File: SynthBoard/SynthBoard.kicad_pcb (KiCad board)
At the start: 2 copper layers, 160 x 80 mm, 113 parts, among them IC1 PIC16F15325-I/P, IC2 MCP6232T-E/SN, IC3 MCP6232T-E/SN, IC4 AS321KTR-E1, IC5 V3340M, IC6 AS321KTR-E1, IC7 4013, J1 Output, J2 Input, J3 Input, J4 Output, J6 A_Power, J7 D_Power, Q1 Q_NPN_ECB, Q18 Q_NPN_ECB, SW1 MFP_240, U1 NJM4558M

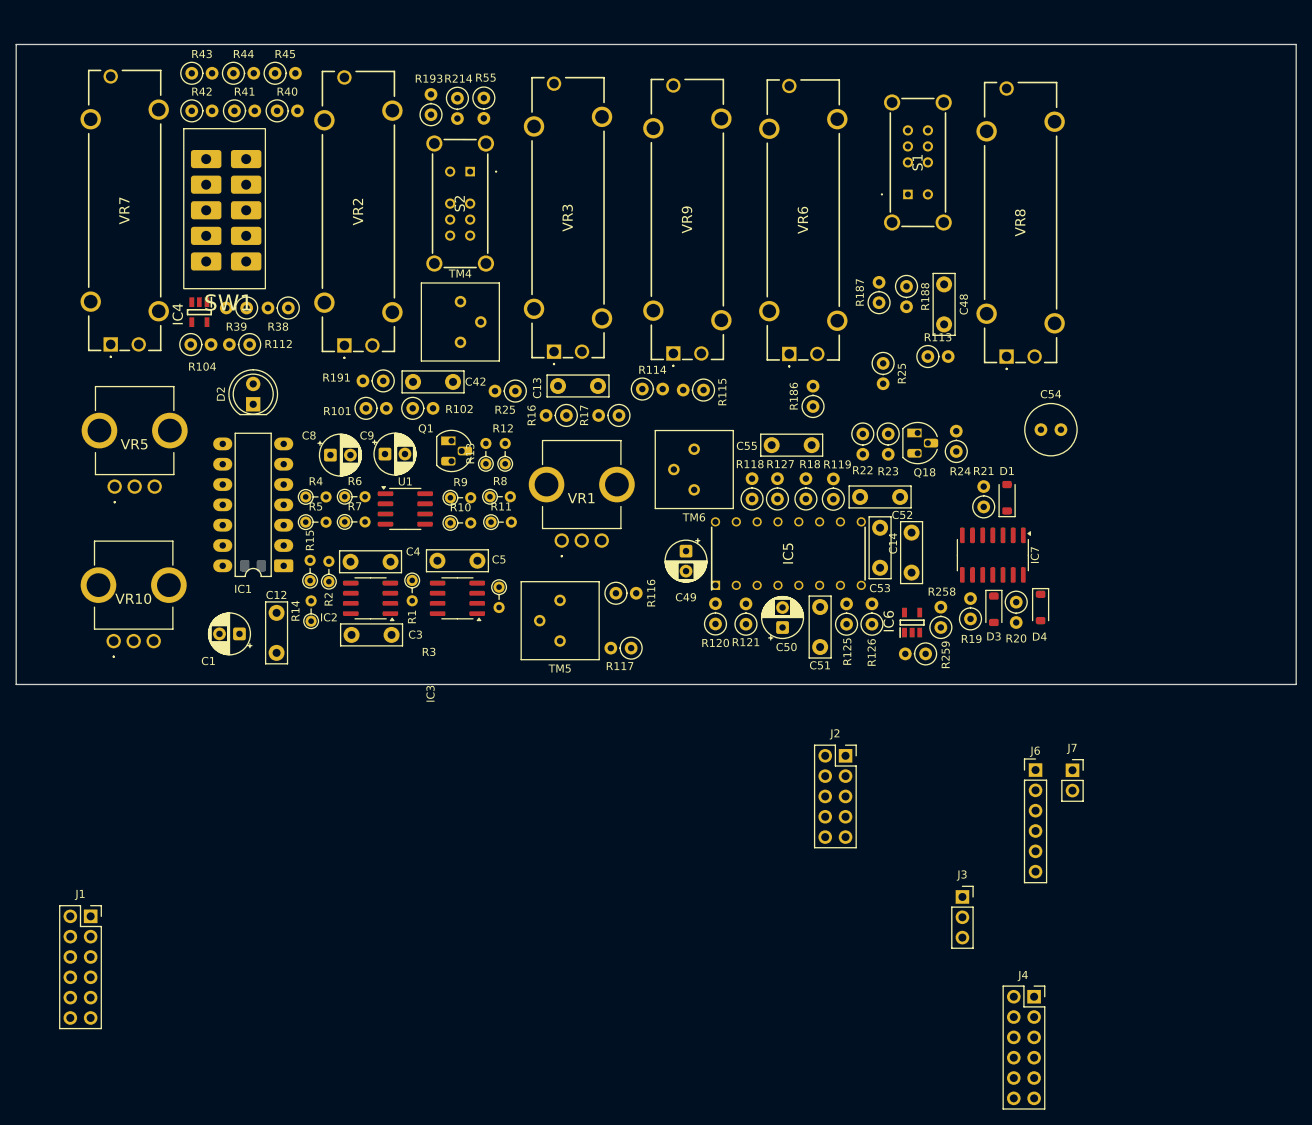
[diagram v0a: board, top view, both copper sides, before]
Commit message: SynthBoard
部品をSMDにしてVCO+LFOを配置した
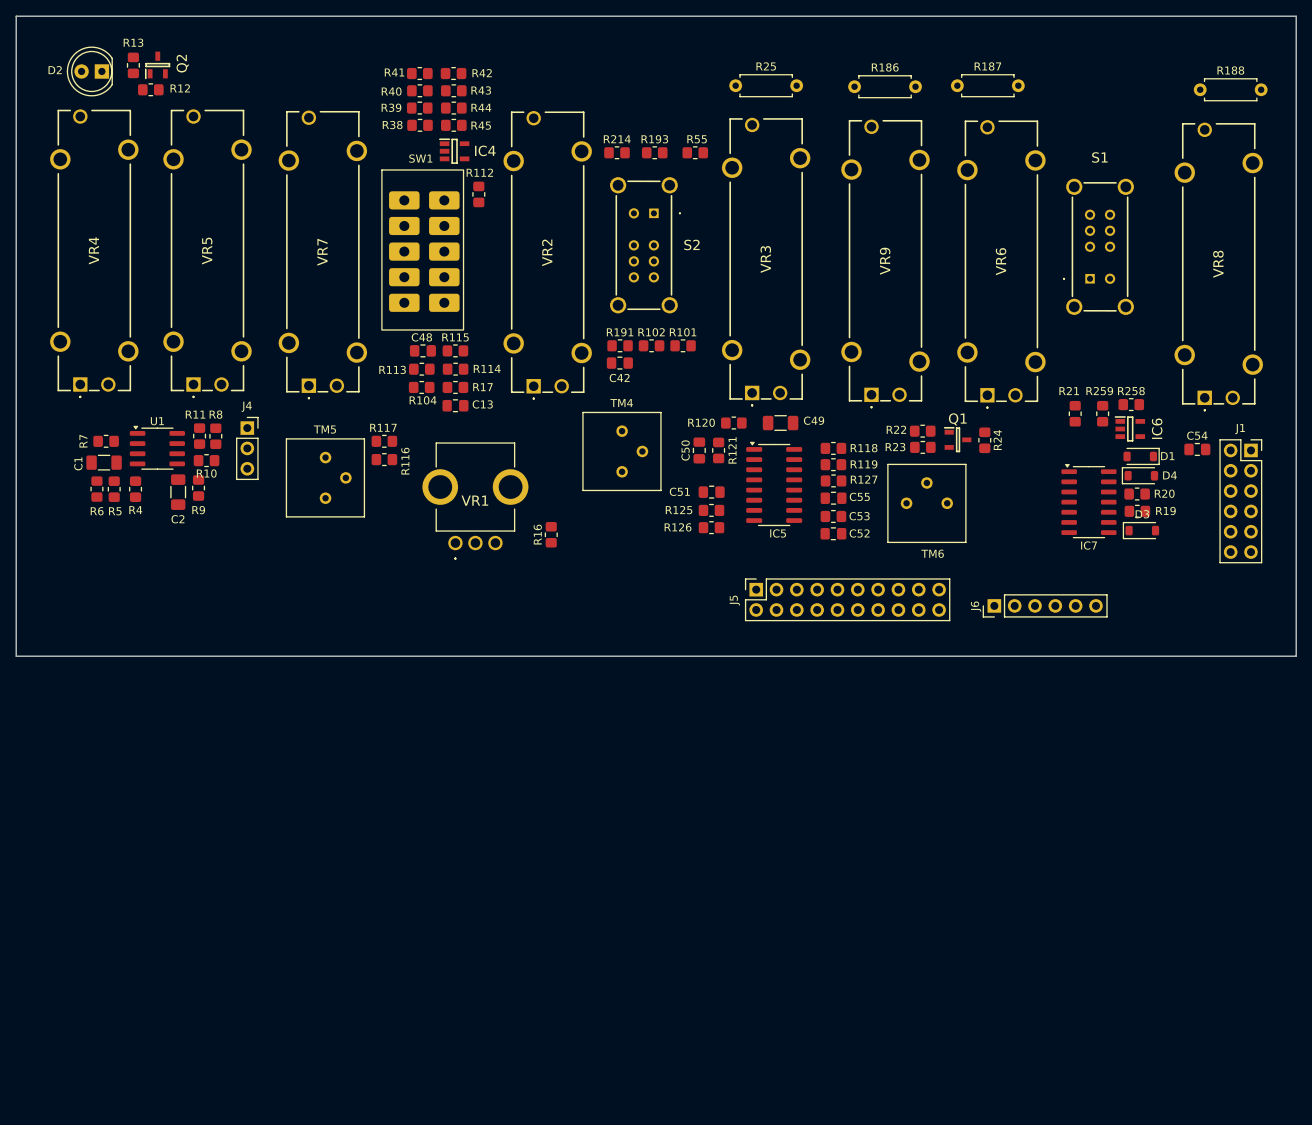
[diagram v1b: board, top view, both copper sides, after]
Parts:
- removed C11: 0.1uF, Capacitor_SMD:C_0805_2012Metric_Pad1.18x1.45mm_HandSolder
- removed C12, C14, C3, C4, C5: 0.01uF, Capacitor_THT:C_Disc_D7.5mm_W2.5mm_P5.00mm
- removed C8, C9: 47uF/16V, Capacitor_THT:CP_Radial_D5.0mm_P2.50mm
- removed IC1: PIC16F15325-I/P, Package_DIP:DIP-14_W7.62mm_LongPads
- removed IC2, IC3: MCP6232T-E/SN, Package_SO:SOIC-8_3.9x4.9mm_P1.27mm
- removed J2: Input, Connector_PinSocket_2.54mm:PinSocket_2x05_P2.54mm_Vertical
- removed J3: Input, Connector_PinSocket_2.54mm:PinSocket_1x03_P2.54mm_Vertical
- removed J7: D_Power, Connector_PinSocket_2.54mm:PinSocket_1x02_P2.54mm_Vertical
- removed Q18: Q_NPN_ECB, Package_TO_SOT_THT:TO-92_HandSolder
- removed R1, R2, R3: 10K, Resistor_THT:R_Axial_DIN0204_L3.6mm_D1.6mm_P2.54mm_Vertical
- removed R14: 1K, Resistor_THT:R_Axial_DIN0204_L3.6mm_D1.6mm_P2.54mm_Vertical
- removed R15: 100, Resistor_THT:R_Axial_DIN0204_L3.6mm_D1.6mm_P2.54mm_Vertical
- removed R18: 1M, Resistor_THT:R_Axial_DIN0207_L6.3mm_D2.5mm_P2.54mm_Vertical
- removed the R25 at (146.9, 86.4)
- removed the R25 at (101.0, 89.9)
- removed VR10: Delay 100KB, SamacSys_parts:RK09D117000B
- added C2: EMK316BBJ476ML-T, Capacitor_SMD:C_1206_3216Metric_Pad1.33x1.80mm_HandSolder, F.Cu at (58.8, 102.5)
- added J5: DigiConn, Connector_PinSocket_2.54mm:PinSocket_2x10_P2.54mm_Vertical, F.Cu at (131.1, 114.7)
- added Q2: 2SC1623(RANGE:300-400), SamacSys_parts:SOT95P237X125-3N, F.Cu at (56.3, 49.1)
- added R25: 390K, Resistor_THT:R_Axial_DIN0207_L6.3mm_D2.5mm_P7.62mm_Horizontal, F.Cu at (128.5, 51.7)
- added VR4: Rate 100KB, SamacSys_parts:PTA20432010CIB104, F.Cu at (46.6, 89.0)
- C1: value 10uF/16V -> EMK316BBJ476ML-T; footprint Capacitor_THT:CP_Radial_D5.0mm_P2.50mm -> Capacitor_SMD:C_1206_3216Metric_Pad1.33x1.80mm_HandSolder
- C13: value 0.001uF -> CL21C102JBCNNNC; footprint Capacitor_THT:C_Disc_D7.5mm_W2.5mm_P5.00mm -> Capacitor_SMD:C_0805_2012Metric_Pad1.18x1.45mm_HandSolder
- C42, C48, C55: value 0.01uF -> 0805B103J500NT; footprint Capacitor_THT:C_Disc_D7.5mm_W2.5mm_P5.00mm -> Capacitor_SMD:C_0805_2012Metric_Pad1.18x1.45mm_HandSolder
- C49: value 47uF/16V -> C3216X5R1E476MTJ00E; footprint Capacitor_THT:CP_Radial_D5.0mm_P2.50mm -> Capacitor_SMD:C_1206_3216Metric_Pad1.33x1.80mm_HandSolder
- C50: value 2.2uF/50V -> CL21B225KAFNNNE; footprint Capacitor_THT:CP_Radial_D5.0mm_P2.50mm -> Capacitor_SMD:C_0805_2012Metric_Pad1.18x1.45mm_HandSolder
- C51, C52: value 0.01uF -> CL21C102JBCNNNC; footprint Capacitor_THT:C_Disc_D7.5mm_W2.5mm_P5.00mm -> Capacitor_SMD:C_0805_2012Metric_Pad1.18x1.45mm_HandSolder
- C53: value 1000pF -> CL21C102JBCNNNC; footprint Capacitor_THT:C_Disc_D7.5mm_W2.5mm_P5.00mm -> Resistor_SMD:R_0805_2012Metric_Pad1.20x1.40mm_HandSolder
- C54: value 10uF/16VBP -> CL21A106KAYNNNE; footprint Capacitor_THT:C_Radial_D6.3mm_H7.0mm_P2.50mm -> Capacitor_SMD:C_0805_2012Metric_Pad1.18x1.45mm_HandSolder
- IC4, IC6: value AS321KTR-E1 -> AS321KTR-G1
- IC5: footprint SamacSys_parts:DIP794W56P260L1905H432Q16N -> Package_SO:SOP-16_3.9x9.9mm_P1.27mm
- IC7: value 4013 -> HEF4013BT,653
- J4: value Output -> Conn_01x03; footprint Connector_PinSocket_2.54mm:PinSocket_2x06_P2.54mm_Vertical -> Connector_PinSocket_2.54mm:PinSocket_1x03_P2.54mm_Vertical
- Q1: value Q_NPN_ECB -> 2SC1623(RANGE:300-400); footprint Package_TO_SOT_THT:TO-92L_HandSolder -> SamacSys_parts:SOT95P237X125-3N
- R10: value 10K -> 0805W8F1002T5E; footprint Resistor_THT:R_Axial_DIN0204_L3.6mm_D1.6mm_P2.54mm_Vertical -> Resistor_SMD:R_0805_2012Metric_Pad1.20x1.40mm_HandSolder
- R101: value 56K -> 0805W8J0563T5E; footprint Resistor_THT:R_Axial_DIN0207_L6.3mm_D2.5mm_P2.54mm_Vertical -> Resistor_SMD:R_0805_2012Metric_Pad1.20x1.40mm_HandSolder
- R102: value 390K -> 0805W8J0394T5E; footprint Resistor_THT:R_Axial_DIN0207_L6.3mm_D2.5mm_P2.54mm_Vertical -> Resistor_SMD:R_0805_2012Metric_Pad1.20x1.40mm_HandSolder
- R104: value 220K -> 0805W8F2203T5E; footprint Resistor_THT:R_Axial_DIN0207_L6.3mm_D2.5mm_P2.54mm_Vertical -> Resistor_SMD:R_0805_2012Metric_Pad1.20x1.40mm_HandSolder
- R11: value 1.2K -> 0805W8F1201T5E; footprint Resistor_THT:R_Axial_DIN0204_L3.6mm_D1.6mm_P2.54mm_Vertical -> Resistor_SMD:R_0805_2012Metric_Pad1.20x1.40mm_HandSolder
- R112, R114, R116, R191: value 100K -> 0805W8J0104T5E; footprint Resistor_THT:R_Axial_DIN0207_L6.3mm_D2.5mm_P2.54mm_Vertical -> Resistor_SMD:R_0805_2012Metric_Pad1.20x1.40mm_HandSolder
- R113, R127: value 560 -> 0805W8F5600T5E; footprint Resistor_THT:R_Axial_DIN0207_L6.3mm_D2.5mm_P2.54mm_Vertical -> Resistor_SMD:R_0805_2012Metric_Pad1.20x1.40mm_HandSolder
- R115: value 560K -> 0805W8F5603T5E; footprint Resistor_THT:R_Axial_DIN0207_L6.3mm_D2.5mm_P2.54mm_Vertical -> Resistor_SMD:R_0805_2012Metric_Pad1.20x1.40mm_HandSolder
- R117: value 270K -> 0805W8F2703T5E; footprint Resistor_THT:R_Axial_DIN0207_L6.3mm_D2.5mm_P2.54mm_Vertical -> Resistor_SMD:R_0805_2012Metric_Pad1.20x1.40mm_HandSolder
- R118: value 1.8K -> 0805W8F1801T5E; footprint Resistor_THT:R_Axial_DIN0207_L6.3mm_D2.5mm_P2.54mm_Vertical -> Resistor_SMD:R_0805_2012Metric_Pad1.20x1.40mm_HandSolder
- R119, R125: value 1.5M -> 0805W8F1504T5E; footprint Resistor_THT:R_Axial_DIN0207_L6.3mm_D2.5mm_P2.54mm_Vertical -> Resistor_SMD:R_0805_2012Metric_Pad1.20x1.40mm_HandSolder
- R12, R4, R9: value 100K -> 0805W8J0104T5E; footprint Resistor_THT:R_Axial_DIN0204_L3.6mm_D1.6mm_P2.54mm_Vertical -> Resistor_SMD:R_0805_2012Metric_Pad1.20x1.40mm_HandSolder
- R120: value 28K -> 0805W8F2802T5E; footprint Resistor_THT:R_Axial_DIN0207_L6.3mm_D2.5mm_P2.54mm_Vertical -> Resistor_SMD:R_0805_2012Metric_Pad1.20x1.40mm_HandSolder
- R121: value 5.6K -> 0805W8F5601T5E; footprint Resistor_THT:R_Axial_DIN0207_L6.3mm_D2.5mm_P2.54mm_Vertical -> Resistor_SMD:R_0805_2012Metric_Pad1.20x1.40mm_HandSolder
- R126, R16, R214, R22: value 10K -> 0805W8F1002T5E; footprint Resistor_THT:R_Axial_DIN0207_L6.3mm_D2.5mm_P2.54mm_Vertical -> Resistor_SMD:R_0805_2012Metric_Pad1.20x1.40mm_HandSolder
- R13: value 2.2K -> 0805W8F2201T5E; footprint Resistor_THT:R_Axial_DIN0204_L3.6mm_D1.6mm_P2.54mm_Vertical -> Resistor_SMD:R_0805_2012Metric_Pad1.20x1.40mm_HandSolder
- R17: value 1M -> 0805W8F1004T5E; footprint Resistor_THT:R_Axial_DIN0207_L6.3mm_D2.5mm_P2.54mm_Vertical -> Resistor_SMD:R_0805_2012Metric_Pad1.20x1.40mm_HandSolder
- R186, R187, R188: footprint Resistor_THT:R_Axial_DIN0207_L6.3mm_D2.5mm_P2.54mm_Vertical -> Resistor_THT:R_Axial_DIN0207_L6.3mm_D2.5mm_P7.62mm_Horizontal
- R19: value 47K -> 0805W8F4702T5E; footprint Resistor_THT:R_Axial_DIN0207_L6.3mm_D2.5mm_P2.54mm_Vertical -> Resistor_SMD:R_0805_2012Metric_Pad1.20x1.40mm_HandSolder
- R193, R259: value 33K -> 0805W8F3302T5E; footprint Resistor_THT:R_Axial_DIN0207_L6.3mm_D2.5mm_P2.54mm_Vertical -> Resistor_SMD:R_0805_2012Metric_Pad1.20x1.40mm_HandSolder
- R20, R21: value 47k -> 0805W8F4702T5E; footprint Resistor_THT:R_Axial_DIN0207_L6.3mm_D2.5mm_P2.54mm_Vertical -> Resistor_SMD:R_0805_2012Metric_Pad1.20x1.40mm_HandSolder
- R23: value 1K -> 0805W8F1001T5E; footprint Resistor_THT:R_Axial_DIN0207_L6.3mm_D2.5mm_P2.54mm_Vertical -> Resistor_SMD:R_0805_2012Metric_Pad1.20x1.40mm_HandSolder
- R24: value 68K -> 0805W8F6802T5E; footprint Resistor_THT:R_Axial_DIN0207_L6.3mm_D2.5mm_P2.54mm_Vertical -> Resistor_SMD:R_0805_2012Metric_Pad1.20x1.40mm_HandSolder
- R258: value 470k -> 0805w8f4703t5e; footprint Resistor_THT:R_Axial_DIN0207_L6.3mm_D2.5mm_P2.54mm_Vertical -> Resistor_SMD:R_0805_2012Metric_Pad1.20x1.40mm_HandSolder
- R38, R39, R40, R41, R42, R43, R44, R45: value 200K -> 0805W8F2003T5E; footprint Resistor_THT:R_Axial_DIN0207_L6.3mm_D2.5mm_P2.54mm_Vertical -> Resistor_SMD:R_0805_2012Metric_Pad1.20x1.40mm_HandSolder
- R5: value 30K -> 0805W8F3002T5E; footprint Resistor_THT:R_Axial_DIN0204_L3.6mm_D1.6mm_P2.54mm_Vertical -> Resistor_SMD:R_0805_2012Metric_Pad1.20x1.40mm_HandSolder
- R55: value 50K -> ARG05DTC5002; footprint Resistor_THT:R_Axial_DIN0207_L6.3mm_D2.5mm_P2.54mm_Vertical -> Resistor_SMD:R_0805_2012Metric_Pad1.20x1.40mm_HandSolder
- R6: value 20K -> 0805W8F2002T5E; footprint Resistor_THT:R_Axial_DIN0204_L3.6mm_D1.6mm_P2.54mm_Vertical -> Resistor_SMD:R_0805_2012Metric_Pad1.20x1.40mm_HandSolder
- R7, R8: value 100 -> 0805W8F1000T5E; footprint Resistor_THT:R_Axial_DIN0204_L3.6mm_D1.6mm_P2.54mm_Vertical -> Resistor_SMD:R_0805_2012Metric_Pad1.20x1.40mm_HandSolder
- TM4, TM5: value 50K -> G43BT-B503
- U1: value NJM4558M -> TJM4558CDT
- VR5: value Rate 100KB -> Delay 100KB; footprint SamacSys_parts:RK09D117000B -> SamacSys_parts:PTA20432010CIB104
- moved J1 156.3 mm to (192.9, 97.3)
- moved J4 121.3 mm to (67.5, 94.5)
- moved R13 66.5 mm to (53.2, 49.1), turned to -90 degrees
- moved C48 65.7 mm to (89.4, 84.8), turned to 0 degrees
- moved R12 64.4 mm to (55.4, 52.2), turned to 0 degrees
- moved Q1 63.3 mm to (156.3, 96.0), turned to 0 degrees
- moved R113 63.3 mm to (89.3, 87.1), turned to 180 degrees
- moved D2 45.7 mm to (49.3, 49.9), turned to 180 degrees
- moved R188 44.2 mm to (186.6, 52.2), turned to 0 degrees
- moved R186 40.3 mm to (143.4, 51.8), turned to 0 degrees
- moved R117 40.3 mm to (84.6, 96.1)
- moved R11 38.0 mm to (61.5, 95.5), turned to 90 degrees
- moved R101 37.7 mm to (121.9, 84.2), turned to 0 degrees
- moved IC4 37.7 mm to (93.4, 59.9), turned to 0 degrees
- moved R259 37.3 mm to (174.4, 92.7), turned to -90 degrees
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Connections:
- C1 pad 1: +5VD -> Net-(C1-Pad1)
- C1 pad 2: GND -> Net-(U1A-+)
- J4 pad 2: Sine -> Triangle
- J4 pad 3: Triangle -> GNDA
- Q1 pad 1: GNDA -> Net-(Q1-B)
- Q1 pad 2: Net-(Q1-C) -> GNDA
- Q1 pad 3: Net-(Q1-B) -> VPseparate
- R12 pad 2: Net-(Q1-B) -> Net-(Q2-B)
- R13 pad 1: Net-(Q1-C) -> Net-(Q2-C)
- R22 pad 2: Net-(Q18-B) -> Net-(Q1-B)
- R23 pad 2: Net-(Q18-B) -> Net-(Q1-B)
- R5 pad 2: Net-(C8-Pad1) -> Net-(C1-Pad1)
- R6 pad 1: Net-(C8-Pad1) -> Net-(C1-Pad1)
- VR5 pad 1: GND -> GNDD
- VR5 pad 2: Rate -> Delay
- VR5 pad MH1: GND -> GNDA
- VR5 pad MH2: GND -> GNDA

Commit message: SynthBoard
アナログのみ一通り設置 デジタルはなし
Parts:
- removed TM4, TM5: G43BT-B503, Potentiometer_THT:Potentiometer_Bourns_3386P_Vertical
- removed TM6: 500, Potentiometer_THT:Potentiometer_Bourns_3386P_Vertical
- added C10: 0805B221K500NT, Capacitor_SMD:C_0805_2012Metric_Pad1.18x1.45mm_HandSolder, F.Cu at (213.5, 104.0)
- added C11: 0805B221K500NT, Capacitor_SMD:C_0805_2012Metric_Pad1.18x1.45mm_HandSolder, F.Cu at (189.7, 101.7)
- added C3: CL21A106KAYNNNE, Capacitor_SMD:C_0805_2012Metric_Pad1.18x1.45mm_HandSolder, F.Cu at (203.1, 94.6)
- added C4: 0805B221K500NT, Capacitor_SMD:C_0805_2012Metric_Pad1.18x1.45mm_HandSolder, F.Cu at (203.1, 103.3)
- added C5: CL21A106KAYNNNE, Capacitor_SMD:C_0805_2012Metric_Pad1.18x1.45mm_HandSolder, F.Cu at (252.6, 95.6)
- added C6: CL21A106KAYNNNE, Capacitor_SMD:C_0805_2012Metric_Pad1.18x1.45mm_HandSolder, F.Cu at (252.6, 97.8)
- added C7: CL21B105KBFNNNE, Capacitor_SMD:C_0805_2012Metric_Pad1.18x1.45mm_HandSolder, F.Cu at (269.7, 107.6)
- added C8: 0805B221K500NT, Capacitor_SMD:C_0805_2012Metric_Pad1.18x1.45mm_HandSolder, F.Cu at (225.8, 103.6)
- added C9: CL21B105KBFNNNE, Capacitor_SMD:C_0805_2012Metric_Pad1.18x1.45mm_HandSolder, F.Cu at (279.8, 110.7)
- added IC1: AS321KTR-G1, SamacSys_parts:SOT95P282X145-5N, F.Cu at (275.1, 84.5)
- added IC2: AS321KTR-G1, SamacSys_parts:SOT95P282X145-5N, F.Cu at (275.7, 107.6)
- added J10: AudioOut, Connector_PinHeader_2.54mm:PinHeader_1x02_P2.54mm_Vertical, F.Cu at (284.0, 108.8)
- added J11: VCF_ResoWav, Connector_PinSocket_2.54mm:PinSocket_1x02_P2.54mm_Vertical, F.Cu at (232.8, 113.2)
- added J7: Input, Connector_PinSocket_2.54mm:PinSocket_2x06_P2.54mm_Vertical, F.Cu at (186.6, 115.6)
- added J8: AudioIn, Connector_PinSocket_2.54mm:PinSocket_1x02_P2.54mm_Vertical, F.Cu at (246.6, 113.3)
- added J9: VCAEnv, Connector_PinSocket_2.54mm:PinSocket_1x02_P2.54mm_Vertical, F.Cu at (269.6, 52.1)
- added Q3: 2SA812, SamacSys_parts:SOT95P240X120-3N, F.Cu at (273.9, 93.0)
- added Q4: 2SC1623(RANGE:300-400), SamacSys_parts:SOT95P237X125-3N, F.Cu at (278.0, 89.0)
- added Q6: 2SA812, SamacSys_parts:SOT95P240X120-3N, F.Cu at (289.3, 49.8)
- added Q7: 2SA812, SamacSys_parts:SOT95P240X120-3N, F.Cu at (255.1, 52.6)
- added Q8: 2SA812, SamacSys_parts:SOT95P240X120-3N, F.Cu at (228.6, 48.9)
- added R1: 0805W8J0104T5E, Resistor_SMD:R_0805_2012Metric_Pad1.20x1.40mm_HandSolder, F.Cu at (207.4, 107.6)
- added R14: 0805W8F5600T5E, Resistor_SMD:R_0805_2012Metric_Pad1.20x1.40mm_HandSolder, F.Cu at (203.1, 101.1)
- added R15: 0805W8F5600T5E, Resistor_SMD:R_0805_2012Metric_Pad1.20x1.40mm_HandSolder, F.Cu at (225.8, 101.2)
- added R18: 0805W8F5600T5E, Resistor_SMD:R_0805_2012Metric_Pad1.20x1.40mm_HandSolder, F.Cu at (203.1, 99.1)
- added R2: 0805W8J0104T5E, Resistor_SMD:R_0805_2012Metric_Pad1.20x1.40mm_HandSolder, F.Cu at (203.1, 96.9)
- added R26: 0805W8F5600T5E, Resistor_SMD:R_0805_2012Metric_Pad1.20x1.40mm_HandSolder, F.Cu at (225.8, 99.1)
- added R27: 0805W8F6802T5E, Resistor_SMD:R_0805_2012Metric_Pad1.20x1.40mm_HandSolder, F.Cu at (203.2, 105.5)
- added R28: 0805W8F6802T5E, Resistor_SMD:R_0805_2012Metric_Pad1.20x1.40mm_HandSolder, F.Cu at (225.8, 105.9)
- added R29: 0805W8F1002T5E, Resistor_SMD:R_0805_2012Metric_Pad1.20x1.40mm_HandSolder, F.Cu at (189.8, 108.2)
- added R3: 0805W8J0104T5E, Resistor_SMD:R_0805_2012Metric_Pad1.20x1.40mm_HandSolder, F.Cu at (225.8, 96.4)
- added R30: 0805W8F1002T5E, Resistor_SMD:R_0805_2012Metric_Pad1.20x1.40mm_HandSolder, F.Cu at (220.9, 107.7)
- added R31: 0805W8J0104T5E, Resistor_SMD:R_0805_2012Metric_Pad1.20x1.40mm_HandSolder, F.Cu at (213.5, 96.8)
- added R32: 0805W8J0104T5E, Resistor_SMD:R_0805_2012Metric_Pad1.20x1.40mm_HandSolder, F.Cu at (203.2, 107.7)
- added R33: 0805W8F3302T5E, Resistor_SMD:R_0805_2012Metric_Pad1.20x1.40mm_HandSolder, F.Cu at (255.2, 49.1)
- added R34: 20K, Resistor_THT:R_Axial_DIN0204_L3.6mm_D1.6mm_P7.62mm_Horizontal, F.Cu at (200.4, 53.2)
- added R35: 56K, Resistor_THT:R_Axial_DIN0204_L3.6mm_D1.6mm_P7.62mm_Horizontal, F.Cu at (230.4, 53.6)
- added R36: 39K, Resistor_THT:R_Axial_DIN0204_L3.6mm_D1.6mm_P7.62mm_Horizontal, F.Cu at (242.8, 53.6)
- added R37: 150K, Resistor_THT:R_Axial_DIN0204_L3.6mm_D1.6mm_P7.62mm_Horizontal, F.Cu at (242.8, 49.3)
- added R46: 0805W8F1002T5E, Resistor_SMD:R_0805_2012Metric_Pad1.20x1.40mm_HandSolder, F.Cu at (271.4, 84.4)
- added R47: 0805W8F2702T5E, Resistor_SMD:R_0805_2012Metric_Pad1.20x1.40mm_HandSolder, F.Cu at (278.5, 84.4)
- added R48: 0805W8F4702T5E, Resistor_SMD:R_0805_2012Metric_Pad1.20x1.40mm_HandSolder, F.Cu at (283.8, 96.8)
- added R49: 0805W8F1001T5E, Resistor_SMD:R_0805_2012Metric_Pad1.20x1.40mm_HandSolder, F.Cu at (274.7, 89.0)
- added R50: 0805W8J0104T5E, Resistor_SMD:R_0805_2012Metric_Pad1.20x1.40mm_HandSolder, F.Cu at (277.9, 92.0)
- added R51: 0805W8F1002T5E, Resistor_SMD:R_0805_2012Metric_Pad1.20x1.40mm_HandSolder, F.Cu at (270.8, 93.1)
- added R52: 0805W8J0104T5E, Resistor_SMD:R_0805_2012Metric_Pad1.20x1.40mm_HandSolder, F.Cu at (273.7, 56.4)
- added R53: 0805W8F4702T5E, Resistor_SMD:R_0805_2012Metric_Pad1.20x1.40mm_HandSolder, F.Cu at (256.5, 95.6)
- added R54: 0805W8F1002T5E, Resistor_SMD:R_0805_2012Metric_Pad1.20x1.40mm_HandSolder, F.Cu at (256.5, 97.8)
- added R56: 0805W8F1002T5E, Resistor_SMD:R_0805_2012Metric_Pad1.20x1.40mm_HandSolder, F.Cu at (263.5, 104.0)
- added R57: 0805W8J0104T5E, Resistor_SMD:R_0805_2012Metric_Pad1.20x1.40mm_HandSolder, F.Cu at (274.6, 53.3)
- added R58: 0805W8F5600T5E, Resistor_SMD:R_0805_2012Metric_Pad1.20x1.40mm_HandSolder, F.Cu at (263.5, 108.2)
- added R59: 0805W8F5600T5E, Resistor_SMD:R_0805_2012Metric_Pad1.20x1.40mm_HandSolder, F.Cu at (263.5, 106.0)
- added R60: 0805W8F1002T5E, Resistor_SMD:R_0805_2012Metric_Pad1.20x1.40mm_HandSolder, F.Cu at (274.6, 49.2)
- added R61: 0805W8F1001T5E, Resistor_SMD:R_0805_2012Metric_Pad1.20x1.40mm_HandSolder, F.Cu at (285.6, 49.5)
- added R62: 0805W8F1001T5E, Resistor_SMD:R_0805_2012Metric_Pad1.20x1.40mm_HandSolder, F.Cu at (285.6, 53.3)
- added R63: 0805W8F1002T5E, Resistor_SMD:R_0805_2012Metric_Pad1.20x1.40mm_HandSolder, F.Cu at (263.5, 110.4)
- added R64: 0805W8J0512T5E, Resistor_SMD:R_0805_2012Metric_Pad1.20x1.40mm_HandSolder, F.Cu at (258.6, 112.5)
- added R65: 0805W8F1001T5E, Resistor_SMD:R_0805_2012Metric_Pad1.20x1.40mm_HandSolder, F.Cu at (289.3, 53.0)
- added R66: 0805W8J0104T5E, Resistor_SMD:R_0805_2012Metric_Pad1.20x1.40mm_HandSolder, F.Cu at (272.0, 107.6)
- added R67: 0805W8F1002T5E, Resistor_SMD:R_0805_2012Metric_Pad1.20x1.40mm_HandSolder, F.Cu at (270.9, 110.7)
- added R68: 0805W8F1002T5E, Resistor_SMD:R_0805_2012Metric_Pad1.20x1.40mm_HandSolder, F.Cu at (293.3, 48.8)
- added R69: 0805W8F4702T5E, Resistor_SMD:R_0805_2012Metric_Pad1.20x1.40mm_HandSolder, F.Cu at (275.4, 110.7)
- added R70: 0805W8J0104T5E, Resistor_SMD:R_0805_2012Metric_Pad1.20x1.40mm_HandSolder, F.Cu at (279.9, 108.3)
- added R71: 0805W8F1002T5E, Resistor_SMD:R_0805_2012Metric_Pad1.20x1.40mm_HandSolder, F.Cu at (251.5, 101.7)
- added R72: 0805W8F5600T5E, Resistor_SMD:R_0805_2012Metric_Pad1.20x1.40mm_HandSolder, F.Cu at (251.5, 106.0)
- added R73: 0805W8F5600T5E, Resistor_SMD:R_0805_2012Metric_Pad1.20x1.40mm_HandSolder, F.Cu at (251.5, 103.9)
- added R74: 0805W8J0104T5E, Resistor_SMD:R_0805_2012Metric_Pad1.20x1.40mm_HandSolder, F.Cu at (212.0, 50.4)
- added R75: 0805W8F1002T5E, Resistor_SMD:R_0805_2012Metric_Pad1.20x1.40mm_HandSolder, F.Cu at (251.5, 108.3)
- added R76: 0805W8F2003T5E, Resistor_SMD:R_0805_2012Metric_Pad1.20x1.40mm_HandSolder, F.Cu at (212.0, 46.5)
- added R77: 0805W8J0512T5E, Resistor_SMD:R_0805_2012Metric_Pad1.20x1.40mm_HandSolder, F.Cu at (251.4, 110.5)
- added R78: 0805W8F1002T5E, Resistor_SMD:R_0805_2012Metric_Pad1.20x1.40mm_HandSolder, F.Cu at (217.0, 53.6)
- added R79: 0805W8F1002T5E, Resistor_SMD:R_0805_2012Metric_Pad1.20x1.40mm_HandSolder, F.Cu at (233.8, 108.4)
- added R80: 0805W8F1002T5E, Resistor_SMD:R_0805_2012Metric_Pad1.20x1.40mm_HandSolder, F.Cu at (244.1, 108.9)
- added R81: 0805W8F1001T5E, Resistor_SMD:R_0805_2012Metric_Pad1.20x1.40mm_HandSolder, F.Cu at (222.9, 50.2)
- added R82: 0805W8F1001T5E, Resistor_SMD:R_0805_2012Metric_Pad1.20x1.40mm_HandSolder, F.Cu at (222.9, 52.2)
- added R83: 0805W8F1001T5E, Resistor_SMD:R_0805_2012Metric_Pad1.20x1.40mm_HandSolder, F.Cu at (222.9, 48.0)
- added R84: 0805W8F1002T5E, Resistor_SMD:R_0805_2012Metric_Pad1.20x1.40mm_HandSolder, F.Cu at (233.8, 104.5)
- added R85: 0805W8F1001T5E, Resistor_SMD:R_0805_2012Metric_Pad1.20x1.40mm_HandSolder, F.Cu at (244.1, 105.0)
- added R86: 0805W8J0512T5E, Resistor_SMD:R_0805_2012Metric_Pad1.20x1.40mm_HandSolder, F.Cu at (231.7, 48.8)
- added R87: 0805W8F5600T5E, Resistor_SMD:R_0805_2012Metric_Pad1.20x1.40mm_HandSolder, F.Cu at (213.4, 101.5)
- added R88: 0805W8F5600T5E, Resistor_SMD:R_0805_2012Metric_Pad1.20x1.40mm_HandSolder, F.Cu at (189.8, 99.3)
- added R89: 0805W8F5600T5E, Resistor_SMD:R_0805_2012Metric_Pad1.20x1.40mm_HandSolder, F.Cu at (213.5, 98.9)
- added R90: 0805W8F5600T5E, Resistor_SMD:R_0805_2012Metric_Pad1.20x1.40mm_HandSolder, F.Cu at (189.8, 97.3)
- added R91: 0805W8F6802T5E, Resistor_SMD:R_0805_2012Metric_Pad1.20x1.40mm_HandSolder, F.Cu at (213.4, 106.2)
- added R92: 0805W8F6802T5E, Resistor_SMD:R_0805_2012Metric_Pad1.20x1.40mm_HandSolder, F.Cu at (189.8, 104.0)
- added R93: 0805W8F1002T5E, Resistor_SMD:R_0805_2012Metric_Pad1.20x1.40mm_HandSolder, F.Cu at (213.4, 108.3)
- added R94: 0805W8F1002T5E, Resistor_SMD:R_0805_2012Metric_Pad1.20x1.40mm_HandSolder, F.Cu at (189.8, 106.2)
- added S3: MS2201L6, SamacSys_parts:MS2201L6, F.Cu at (277.2, 68.1)
- added U2: LM13700, Package_SO:SOIC-16_3.9x9.9mm_P1.27mm, F.Cu at (196.4, 101.1)
- added U3: Opamp_Dual, Package_SO:SOIC-8_3.9x4.9mm_P1.27mm, F.Cu at (279.9, 51.1)
- added U4: Opamp_Dual, Package_SO:SOIC-8_3.9x4.9mm_P1.27mm, F.Cu at (217.0, 49.5)
- added U5: LM13700, Package_SO:SOIC-16_3.9x9.9mm_P1.27mm, F.Cu at (219.5, 100.8)
- added U6: Opamp_Dual, Package_SO:SOIC-8_3.9x4.9mm_P1.27mm, F.Cu at (238.9, 106.8)
- added U8: LM13700, Package_SO:SOIC-16_3.9x9.9mm_P1.27mm, F.Cu at (257.2, 105.9)
- added VR10: 3362P-1-503LF, SamacSys_parts:3362P_1, F.Cu at (261.0, 54.6)
- added VR11: Mod 100KA, SamacSys_parts:PTA20432010CIB104, F.Cu at (246.8, 91.0)
- added VR12: KYBD 100KB, SamacSys_parts:PTA20432010CIB104, F.Cu at (260.9, 91.0)
- added VR13: Env 100KB, SamacSys_parts:PTA20432010CIB104, F.Cu at (232.3, 91.0)
- added VR14: 100KA, SamacSys_parts:RK09D117000B, F.Cu at (319.7, 112.9)
- added VR15: Freq 100KB, SamacSys_parts:PTA20432010CIB104, F.Cu at (202.7, 90.9)
- added VR16: 3362P-1-103LF, SamacSys_parts:3362P_1, F.Cu at (235.6, 102.1)
- added VR17: 3362P-1-103LF, SamacSys_parts:3362P_1, F.Cu at (243.2, 102.1)
- added VR18: Resonance 100KB, SamacSys_parts:PTA20432010CIB104, F.Cu at (217.4, 91.0)
- added VR19: 3362P-1-104LF, SamacSys_parts:3362P_1, F.Cu at (279.3, 101.8)
- added VR20: 3362P-1-503LF, SamacSys_parts:3362P_1, F.Cu at (108.1, 101.4)
- added VR21: 3362P-1-503LF, SamacSys_parts:3362P_1, F.Cu at (120.4, 92.9)
- added VR22: AccLevel 10KB, SamacSys_parts:RK09D117000B, F.Cu at (297.8, 112.8)
- added VR23: Attack 100KA, SamacSys_parts:PTA20432010CIB104, F.Cu at (290.9, 57.9)
- added VR24: Decay 100KA, SamacSys_parts:PTA20432010CIB104, F.Cu at (305.5, 57.7)
- added VR25: Sustain 100KB, SamacSys_parts:PTA20432010CIB104, F.Cu at (320.1, 57.7)
- added VR26: Release 100KA, SamacSys_parts:PTA20432010CIB104, F.Cu at (334.7, 57.7)
- added VR27: 3362P-1-104LF, SamacSys_parts:3362P_1, F.Cu at (161.0, 105.9)
- moved C54 42.9 mm to (171.3, 56.9)
- moved J1 33.3 mm to (165.4, 116.0), turned to 90 degrees
- moved R116 29.5 mm to (114.0, 99.1)
- moved R117 29.5 mm to (114.0, 96.9)
- moved J4 28.4 mm to (44.2, 110.7), turned to 90 degrees
- moved R188 17.1 mm to (169.4, 52.1)
- moved J5 15.1 mm to (116.0, 115.3)
- moved J6 14.7 mm to (146.2, 114.8)
- moved C49 9.59 mm to (143.6, 95.0)
- moved C50 9.59 mm to (133.5, 98.4)
- moved C51 9.59 mm to (135.0, 103.6)
- moved C52 9.59 mm to (150.2, 108.8)
- moved C53 9.59 mm to (150.2, 106.7)
- moved C55 9.59 mm to (150.3, 104.4)
- moved IC5 9.59 mm to (142.8, 102.7)
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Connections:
- VR7 pad 3: LFO_Sine -> Sine
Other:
- board size 160 x 80 mm -> 300 x 80 mm
